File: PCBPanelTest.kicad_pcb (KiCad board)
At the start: 2 copper layers, 25.4 x 25.4 mm, 3 parts, among them J1 Conn_01x02_Male

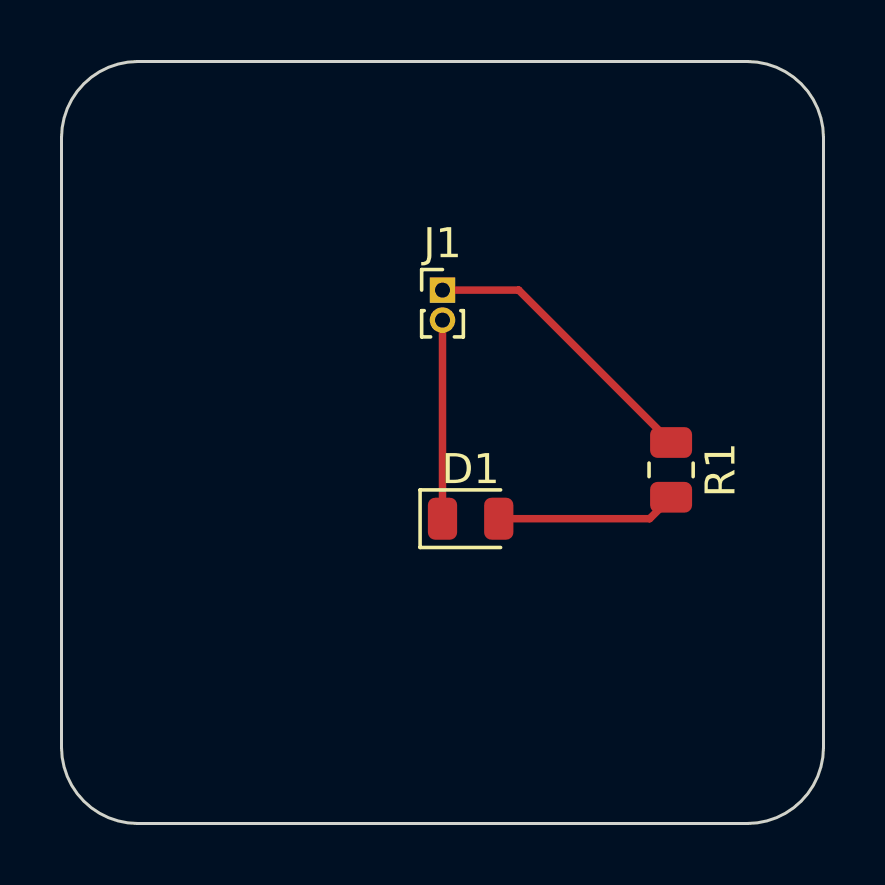
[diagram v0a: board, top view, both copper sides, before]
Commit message: add kibot workflow
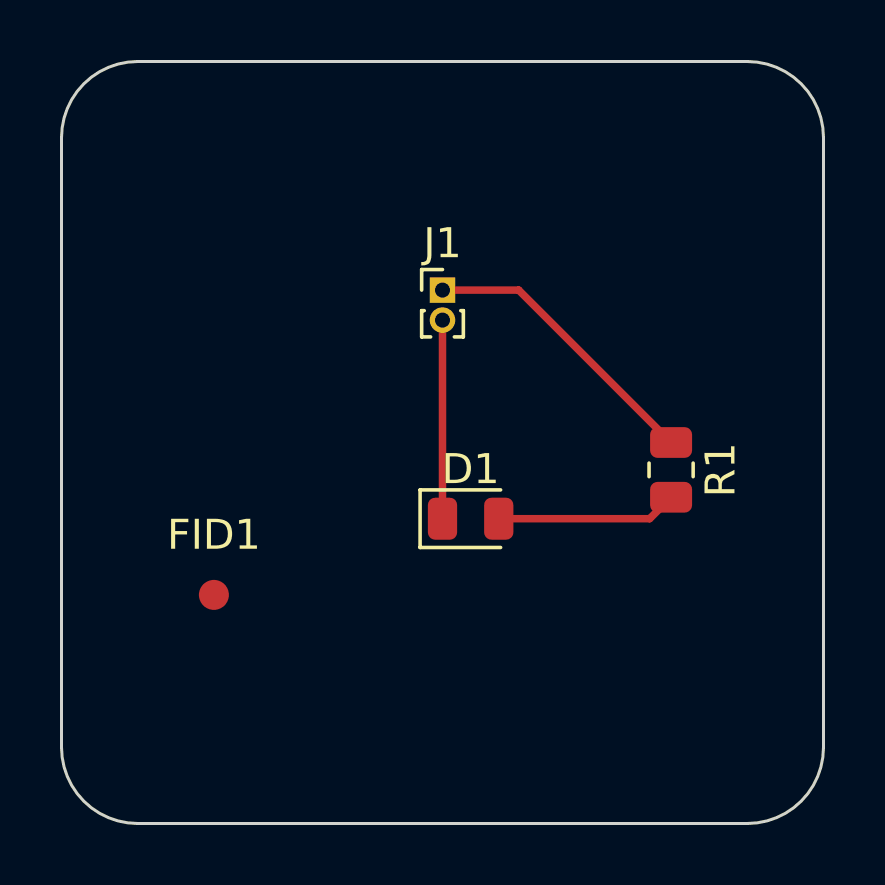
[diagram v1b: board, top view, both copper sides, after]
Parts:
- added FID1: Fiducial, Fiducial:Fiducial_1mm_Mask2mm, F.Cu at (106.7, 94.0)
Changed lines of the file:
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@@
     )
+  )
+  (footprint "Fiducial:Fiducial_1mm_Mask2mm" (layer "F.Cu")
+    (at 106.68 93.98)
+    (descr "Circular Fiducial, 1mm bare copper, 2mm soldermask opening (Level A)")
+    (tags "fiducial")
+    (property "Sheetfile" "PCBPanelTest.kicad_sch")
+    (property "Sheetname" "")
+    (attr smd)
+    (fp_text reference "FID1" (at 0 -2) (layer "F.SilkS")
+      (effects (font (size 1 1) (thickness 0.15)))
+    )
+    (fp_text value "Fiducial" (at 0 2) (layer "F.Fab")
+      (effects (font (size 1 1) (thickness 0.15)))
+    )
+    (fp_text user "${REFERENCE}" (at 0 0) (layer "F.Fab")
+      (effects (font (size 0.4 0.4) (thickness 0.06)))
+    )
+    (fp_circle (center 0 0) (end 1.25 0) (layer "F.CrtYd") (width 0.05) (fill none))
+    (fp_circle (center 0 0) (end 1 0) (layer "F.Fab") (width 0.1) (fill none))
+    (pad "" smd circle (at 0 0) (size 1 1) (layers "F.Cu" "F.Mask")
+      (solder_mask_margin 0.5) (clearance 0.5))
   )
   (gr_line (start 124.46 101.6) (end 104.14 101.6) (layer "Edge.Cuts") (width 0.1))
